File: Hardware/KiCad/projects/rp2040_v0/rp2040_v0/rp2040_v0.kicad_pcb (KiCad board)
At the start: 2 copper layers, 99.6 x 101.6 mm, 133 parts, among them J1 Conn_01x03, J10 Conn_01x01, J11 Conn_01x02, J12 Screw_Terminal_01x02, J13 Conn_02x09_Odd_Even, J14 Conn_02x06_Odd_Even, J15 Conn_01x02, J16 Conn_01x03, J17 Conn_01x03, J18 Conn_01x03, J19 Conn_01x03, J2 Conn_01x02, J20 Conn_01x03, J21 Conn_01x03, J22 Conn_02x05_Odd_Even, J23 Screw_Terminal_01x02, J25 Screw_Terminal_01x02, J27 Screw_Terminal_01x02, J28 Screw_Terminal_01x02, J3 Conn_01x03, J4 Conn_01x01, J5 USB_B_Micro, J6 Conn_01x01, J7 Conn_01x01, J8 Conn_01x03, J9 Conn_01x02, Q1 2N7002, Q2 AO3400A, Q3 2N7002, Q4 AO3400A, Q5 AO3400A, U1 W25Q128JVSIQTR, U12 DRV8837, U2 AMS1117-3.3, U3 RP2040, U4 AMS1117-5.0, U5 BMI088, U6 BMP280, U7 AMS1117-5.0, U8 AMS1117-5.0, X1 X322512MSB4SI

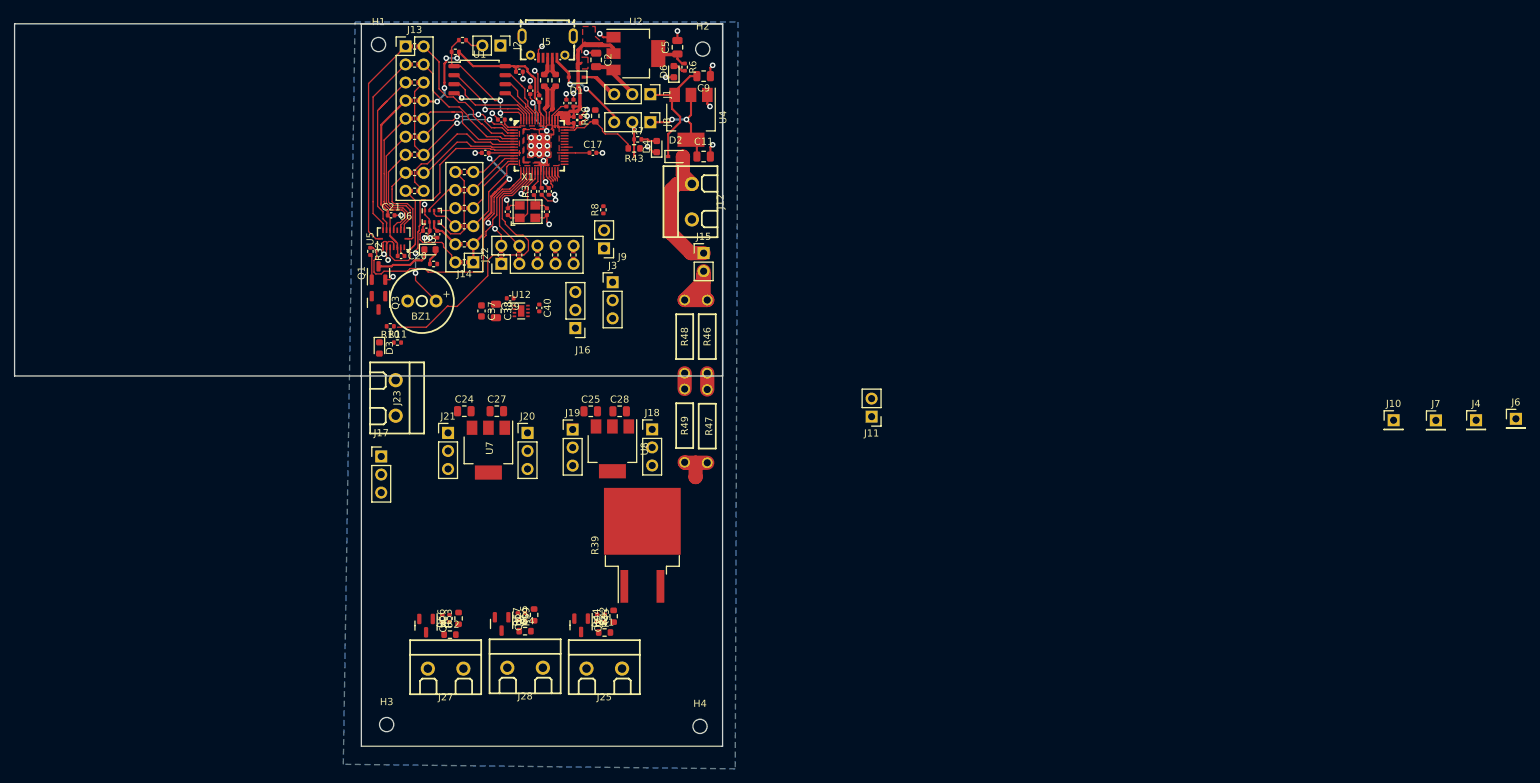
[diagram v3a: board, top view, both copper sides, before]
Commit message: Rev 0 ready to ship! Had to move IMU so board got sloppy. IMU should be in the middle of the board. Glad I caught that.
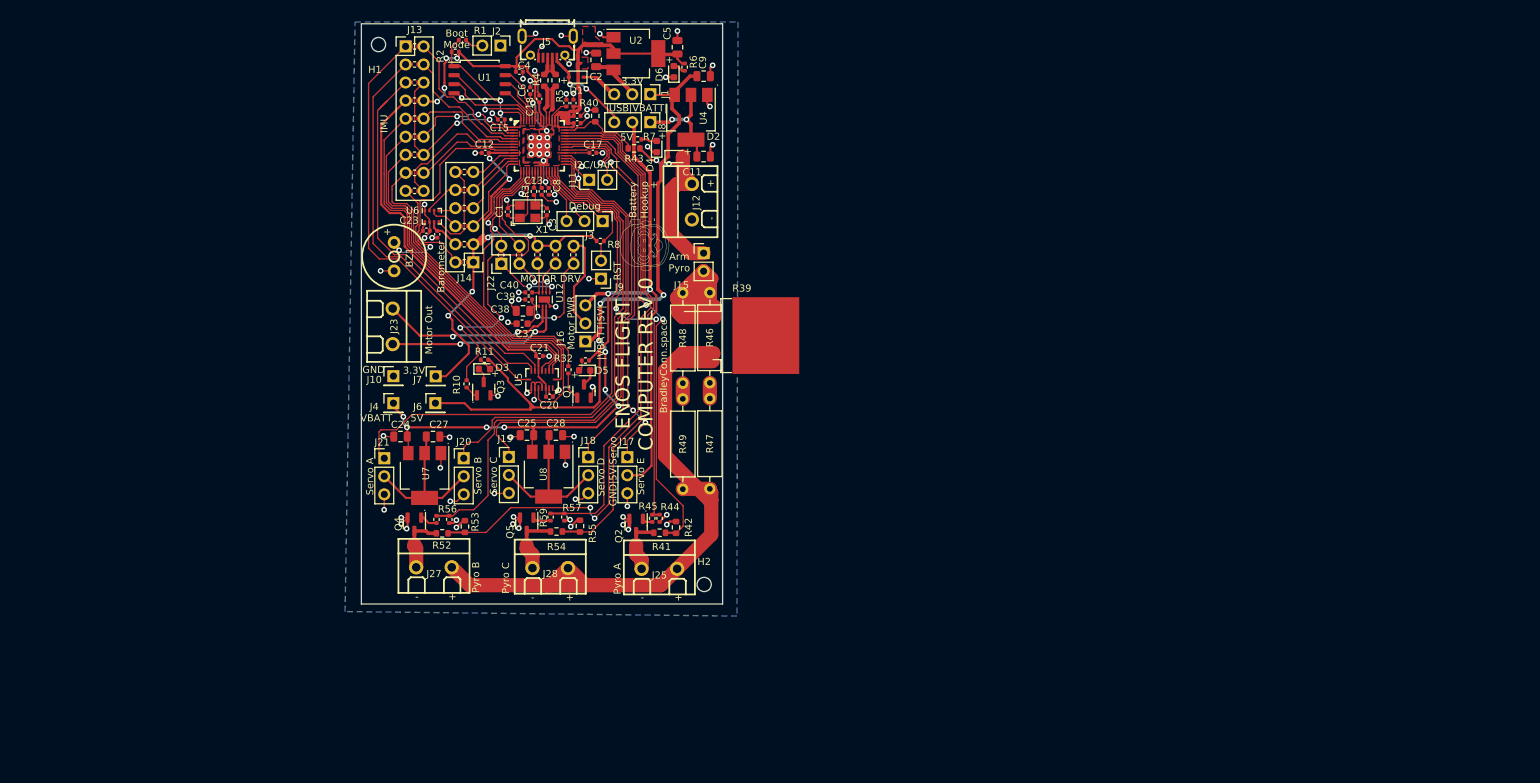
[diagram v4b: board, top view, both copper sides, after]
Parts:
- removed H3, H4: MountingHole, MountingHole:MountingHole_2mm
- added G***: LOGO, LOGO, F.Cu at (149.1, 75.5)
- added G***: LOGO, LOGO, B.Cu at (153.9, 115.7)
- R39: footprint Package_TO_SOT_SMD:TO-263-2 -> Package_TO_SOT_SMD:TO-263-2_TabPin1
- R46, R47, R48, R49: footprint easyeda2kicad:RES-TH_BD2.4-L6.3-P10.30-D0.6 -> Resistor_THT:R_Axial_DIN0309_L9.0mm_D3.2mm_P12.70mm_Horizontal
- moved J4 152.3 mm to (113.6, 97.8)
- moved J6 152.0 mm to (119.5, 97.8)
- moved J10 140.8 mm to (113.6, 94.0)
- moved J7 140.8 mm to (119.5, 94.0)
- moved H2 75.3 mm to (157.3, 123.3)
- moved J11 51.8 mm to (141.1, 66.4), turned to 90 degrees
- moved J17 34.6 mm to (146.5, 105.4)
- moved Q1 33.3 mm to (140.4, 96.1)
- moved R39 32.6 mm to (162.6, 88.3), turned to 0 degrees
- moved R32 32.4 mm to (138.2, 93.1)
- moved C20 28.8 mm to (135.5, 96.9)
- moved C21 28.8 mm to (134.1, 91.2)
- moved U5 28.8 mm to (134.5, 94.5)
- moved D5 27.6 mm to (140.5, 93.2), turned to 180 degrees
- moved R33 25.3 mm to (140.6, 91.8)
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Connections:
- J22 pad 5: Net-(J22-Pad5) -> Net-(C40-Pad1)
- J22 pad 7: Net-(C40-Pad1) -> Net-(J22-Pad7)
- R36 pad 1: Net-(J22-Pad5) -> Net-(J22-Pad7)
- U12 pad 2: Net-(J23-Pad1) -> Net-(J23-Pad2)
- U12 pad 3: Net-(J23-Pad2) -> Net-(J23-Pad1)
- U12 pad 7: Net-(J22-Pad5) -> Net-(J22-Pad7)
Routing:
- net +5V: track 4.93 -> 117.4 mm, vias 0 -> 2
- net Protected_VBATT+: track 17.9 -> 108.2 mm, vias 0 -> 10
- net Armed_Batt+_with_big_pyro_resistor: track 5.23 -> 94.9 mm
- net ADC_1__Pyro_B_Continuity_Check: track 0.00 -> 89.3 mm, vias 0 -> 2
- net Pyro_Control_B: track 0.00 -> 77.5 mm
- net PWM_0_A__Servo_A: track 1.54 -> 76.4 mm
- net ADC_2__Pyro_C_Continuity_Check: track 0.00 -> 73.0 mm
- net ADC_0__Pyro_A_Continuity_Check: track 0.00 -> 69.2 mm, vias 0 -> 2
- net Pyro_Control_C: track 0.00 -> 69.1 mm
- net PWM_1_A__Servo_B: track 0.00 -> 65.2 mm
- net PWM_2_B__Servo_C: track 0.00 -> 65.0 mm, vias 0 -> 2
- net +3.3V: track 122.2 -> 185.0 mm, vias 6 -> 10
- net Pyro_Control_A: track 0.96 -> 60.2 mm, vias 0 -> 2
- net GND: track 74.0 -> 130.1 mm, vias 42 -> 77
- net PWM_3_A__Servo_D: track 0.00 -> 55.0 mm, vias 0 -> 2
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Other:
- board size 99.6 x 101.6 mm -> 50.8 x 81.6 mm
- board text added: "+"
- board text added: "-"
- board text added: "->"
- board text added: "."
- board text added: "3.3V"
- board text added: "3.3v"
- board text added: "5V"
- board text added: "A"
- board text added: "Acc int"
- board text added: "Arm Pyro"
- board text added: "B"
- board text added: "Barometer"
- board text added: "Battery Hookup"
- board text added: "Battery Hookup 3S lipo (2S optional)"
- board text added: "Boot Mode"
- board text added: "BradleyConn.space"
- board text added: "Buzzer"
- board text added: "Debug"
- board text added: "ENOS FLIGHT COMPUTER"
- board text added: "ENOS FLIGHT COMPUTER REV 0"
- board text added: "GND"
- board text added: "GND|5V|Servo"
- board text added: "Gyr int"
- board text added: "I2C/UART"
- board text added: "IMU"
- board text added: "MOTOR DRV"
- board text added: "MTR PWR"
- board text added: "Motor Driver"
- board text added: "Motor Hookup"
- board text added: "Motor Out"
- board text added: "Motor PWR"
- board text added: "Place jumper to change boot mode holds flash CS low"
- board text added: "Power Settings to drive 3.3V net"
- board text added: "Power Settings to drive 5V net"
- board text added: "Power setting to drive motor either 5v net or vbatt"
- board text added: "Pyro A"
- board text added: "Pyro B"
- board text added: "Pyro C"
- board text added: "Pyro Resistors"
- board text added: "Pyros remain unarmed unless jumper connected"
- board text added: "REV 0"
- board text added: "RST"
- board text added: "SLEEP"
- board text added: "Servo A"
- board text added: "Servo B"
- board text added: "Servo C"
- board text added: "Servo D"
- board text added: "Servo E"
- board text added: "Touch the two pins to reset rp2040"
- board text added: "Use jumper to select power setting"
- board text added: "VBATT"
- board text added: "VCC (3.3V)"
- board text added: "VDD (3.3V)"
- board text added: "VDDIO (3.3v)"
- board text added: "cs"
- board text added: "cs Acc"
- board text added: "cs Gyr"
- board text added: "miso"
- board text added: "miso1"
- board text added: "miso2"
- board text added: "mosi"
- board text added: "sck"
- board text added: "sclk"
- board text added: "|5V|PWR|VBATT|"
- board text added: "|SCL/RX|SDA/TX|"
- board text added: "|SWD|GND|SWCLK|"
- board text added: "|Servo A|5V|GND|"
- board text added: "|Servo B|5V|GND|"
- board text added: "|Servo C|5V|GND|"
- board text added: "|Servo D|5V|GND|"
- board text added: "|Servo E|5V|GND|"
- board text added: "|USB|VBATT|"
- board text added: "|VBATT|5V|"
- board text added: "|VBATT|USB|"

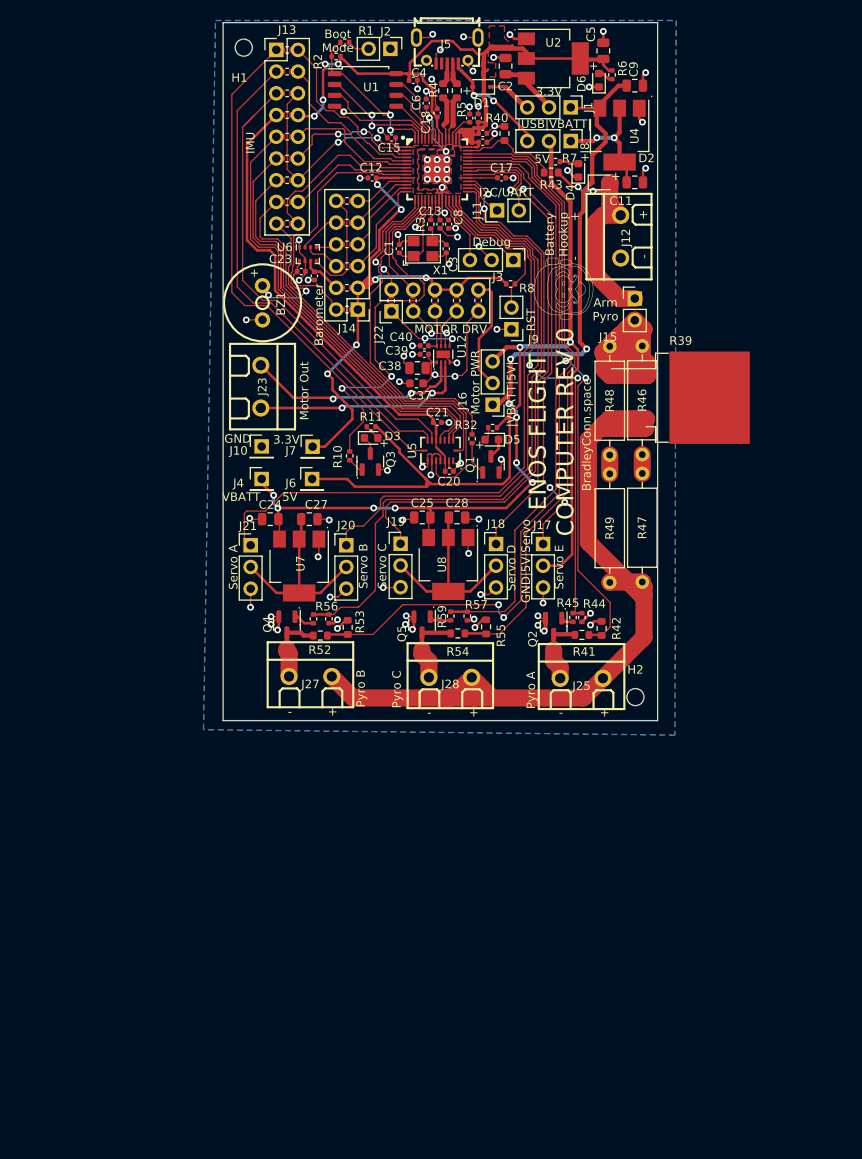
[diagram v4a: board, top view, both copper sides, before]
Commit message: Some minor changes with footprint. Sent to JLCPCB. Official Rev 0!
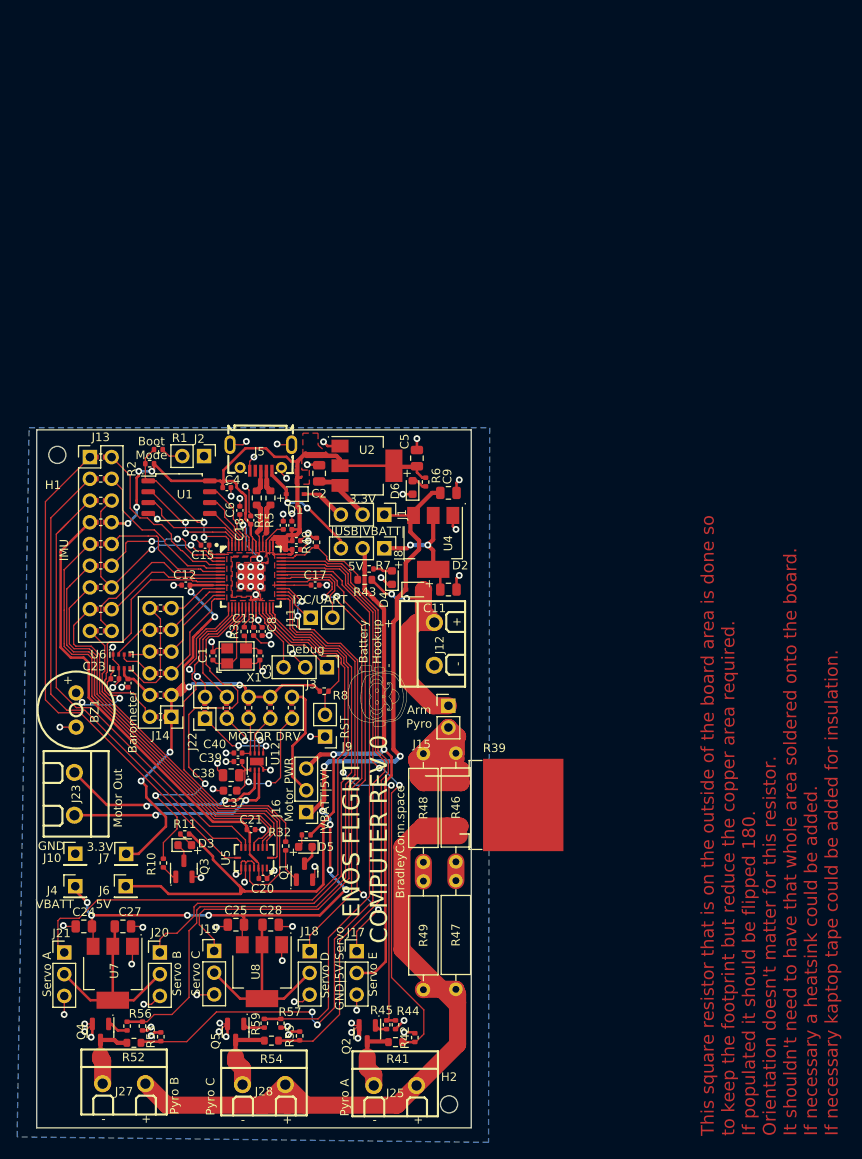
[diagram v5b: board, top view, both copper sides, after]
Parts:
- R39: value 3 -> 3(DNP)
- R40, R42, R53, R55: footprint Resistor_SMD:R_0603_1608Metric -> Resistor_SMD:R_0402_1005Metric
- R46, R47, R48, R49: value DNP -> 2.2
- moved R53 52.6 mm to (101.8, 163.0)
- moved R40 52.6 mm to (120.0, 105.2)
- moved R42 52.6 mm to (131.5, 163.1)
- moved R55 52.6 mm to (118.0, 162.9)
- moved C20 52.4 mm to (113.8, 144.5)
- moved C24 52.4 mm to (92.8, 150.1)
- moved C27 52.4 mm to (97.4, 150.1)
- moved C39 52.4 mm to (110.8, 130.8)
- moved C40 52.4 mm to (110.8, 129.8)
- moved D3 52.4 mm to (104.6, 140.6)
- moved J10 52.4 mm to (91.8, 141.6)
- moved J12 52.4 mm to (133.8, 117.1)
- moved J16 52.4 mm to (118.8, 136.7)
- moved J20 52.4 mm to (101.7, 153.2)
- moved J21 52.4 mm to (90.5, 153.2)
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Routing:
- net GND: track 130.1 -> 129.4 mm
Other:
- board text added: "This square resistor that is on the outside of the board area is done so to keep the footprint but reduce the copper area required. If populated it should be flipped 180. Orientation doesn't matter for this resistor. It shouldn't need to have that whole area soldered onto the board. If necessary a heatsink could be added. If necessary kaptop tape could be added for insulation."
